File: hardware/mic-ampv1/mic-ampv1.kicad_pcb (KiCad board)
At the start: 2 copper layers, 45.2 x 45 mm, 18 parts, among them J1 XLR3_Switched, U1 NE5532

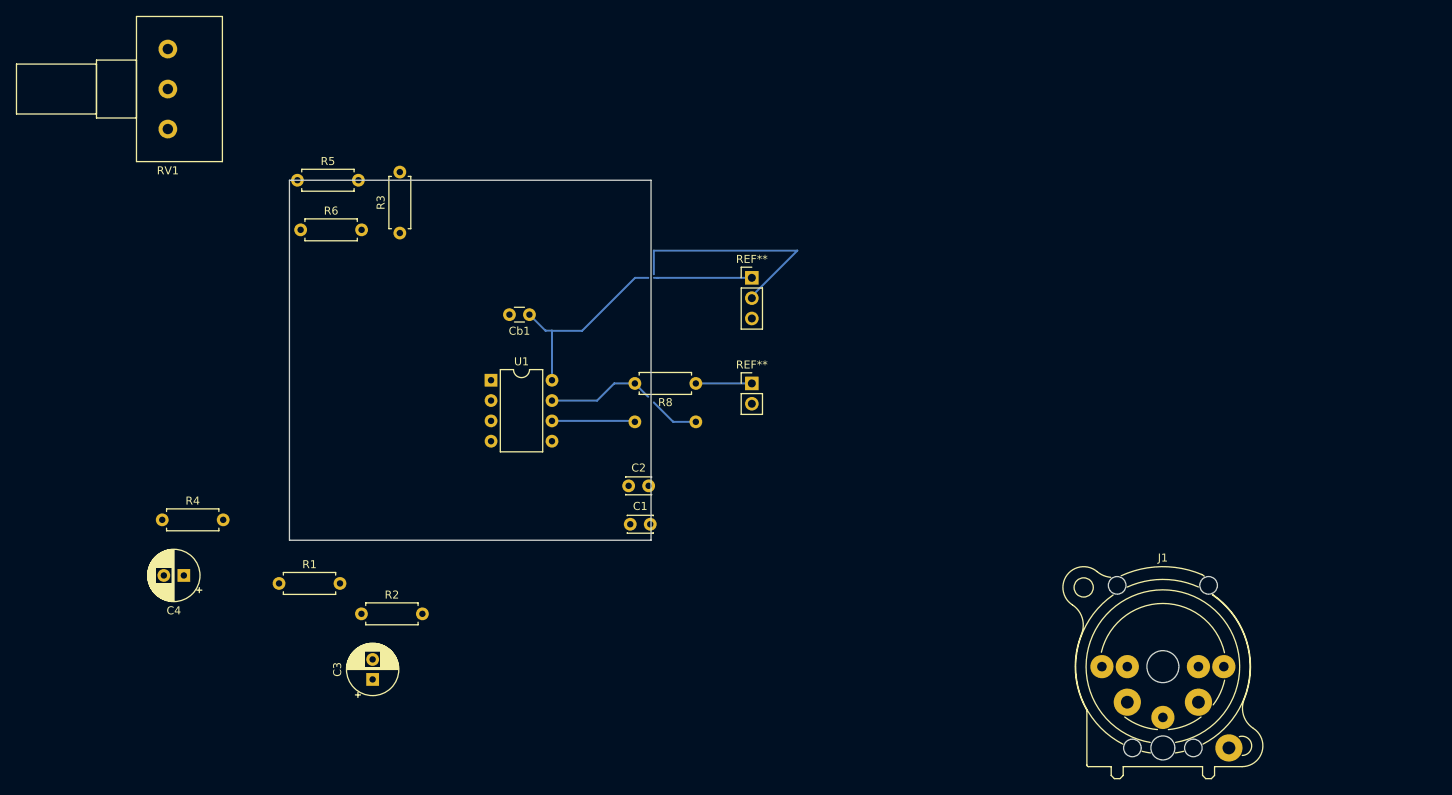
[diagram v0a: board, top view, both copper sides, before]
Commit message: complete pcb for mic
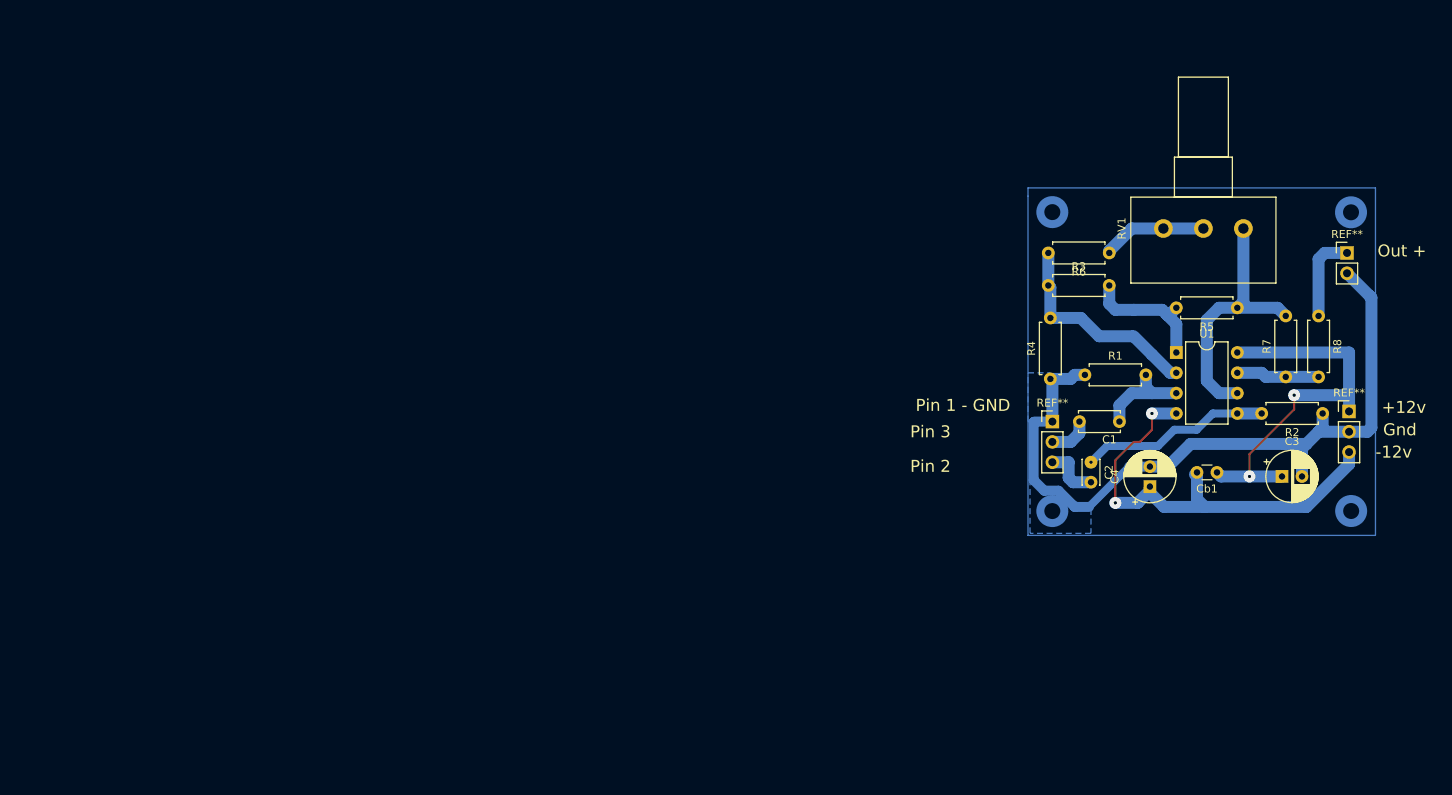
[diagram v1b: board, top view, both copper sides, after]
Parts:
- removed J1: XLR3_Switched, Connector_Audio:Jack_XLR-6.35mm_Neutrik_NCJ6FA-V-0_Vertical
- removed the REF** at (138.2, 72.2)
- added REF**: PinHeader_1x03_P2.54mm_Vertical, Connector_PinHeader_2.54mm:PinHeader_1x03_P2.54mm_Vertical, F.Cu at (175.8, 90.2)
- added REF**: PinHeader_1x03_P2.54mm_Vertical, Connector_PinHeader_2.54mm:PinHeader_1x03_P2.54mm_Vertical, F.Cu at (212.9, 88.9)
- C1: footprint Capacitor_THT:C_Disc_D3.0mm_W2.0mm_P2.50mm -> Capacitor_THT:C_Disc_D5.0mm_W2.5mm_P5.00mm
- R7: moved to F.Cu
- moved RV1 136.3 mm to (199.6, 66.0), turned to 90 degrees
- moved R2 122.7 mm to (209.6, 89.2), turned to 180 degrees
- moved C4 121.3 mm to (188.0, 98.3), turned to 90 degrees
- moved R5 118.6 mm to (198.9, 75.9), turned to 180 degrees
- moved C3 116.5 mm to (204.5, 97.0), turned to 0 degrees
- moved R4 112.4 mm to (175.5, 84.8), turned to 90 degrees
- moved R1 104.1 mm to (179.8, 84.3)
- moved R6 101.1 mm to (182.9, 69.1), turned to 180 degrees
- moved Cb1 88.2 mm to (196.3, 96.5)
- moved U1 85.7 mm to (191.3, 81.5)
- moved R3 81.3 mm to (175.3, 73.2), turned to 0 degrees
- moved R8 78.3 mm to (209.0, 77.0), turned to 270 degrees
- moved REF** 76.2 mm to (212.6, 69.1)
- moved R7 74.0 mm to (204.9, 84.6), turned to 90 degrees
- moved C1 62.5 mm to (184.2, 90.2), turned to 180 degrees
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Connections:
- C3 pad 2: GND -> Gnd
- C4 pad 2: GND -> Gnd
- R1 pad 1: GND -> Gnd
- R2 pad 1: GND -> Gnd
- R4 pad 1: GND -> Gnd
- REF** pad 2: (no net) -> Gnd
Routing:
- net Gnd: track 0.00 -> 97.7 mm
- net -12V: track 29.5 -> 57.2 mm, vias 0 -> 2
- net Net-(R3-Pad1): track 0.00 -> 26.8 mm
- net Net-(C2-Pad1): track 0.00 -> 23.9 mm
- net Net-(R5-Pad1): track 10.4 -> 33.2 mm
- net Net-(R3-Pad2): track 0.00 -> 16.8 mm
- net Net-(R6-Pad1): track 0.00 -> 13.2 mm
- net Net-(C1-Pad1): track 0.00 -> 12.4 mm
- net +12V: track 36.9 -> 49.1 mm, vias 0 -> 2
- net Net-(R7-Pad1): track 19.9 -> 10.4 mm
- net Net-(C1-Pad2): track 0.00 -> 7.06 mm
- net Net-(C2-Pad2): track 0.00 -> 7.00 mm
- net (no net): track 7.00 -> 11.0 mm
- added copper zone on B.Cu, net Gnd
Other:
- board outline removed
- board text added: "+12v"
- board text added: "-12v"
- board text added: "Gnd"
- board text added: "Out +"
- board text added: "Pin 1 - GND"
- board text added: "Pin 2"
- board text added: "Pin 3"

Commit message: Updated mic pre-amp. Longer board to help with layout. increase gain by changing R6 ->47 Ohm
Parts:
- C1: footprint Capacitor_THT:C_Disc_D5.0mm_W2.5mm_P5.00mm -> Capacitor_THT:C_Disc_D3.0mm_W2.0mm_P2.50mm
- R6: value 270 -> 47
- moved C3 7.47 mm to (204.5, 104.5)
- moved C4 7.38 mm to (188.0, 105.7)
- moved C2 3.50 mm to (180.6, 98.8)
- moved C1 1.35 mm to (185.5, 90.2)
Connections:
- R8 pad 1: (no net) -> Out
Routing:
- net Gnd: track 97.7 -> 125.3 mm
- net -12V: track 57.2 -> 73.2 mm
- net Out: track 0.00 -> 11.0 mm
- net (no net): track 11.0 -> 0.00 mm
- net +12V: track 49.1 -> 54.2 mm
- net Net-(C1-Pad2): track 7.06 -> 10.9 mm
- net Net-(U1B-+): track 23.9 -> 21.0 mm
- net Net-(C2-Pad2): track 7.00 -> 9.19 mm
- net Net-(U1A-+): track 12.4 -> 11.8 mm
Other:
- net class Default removed

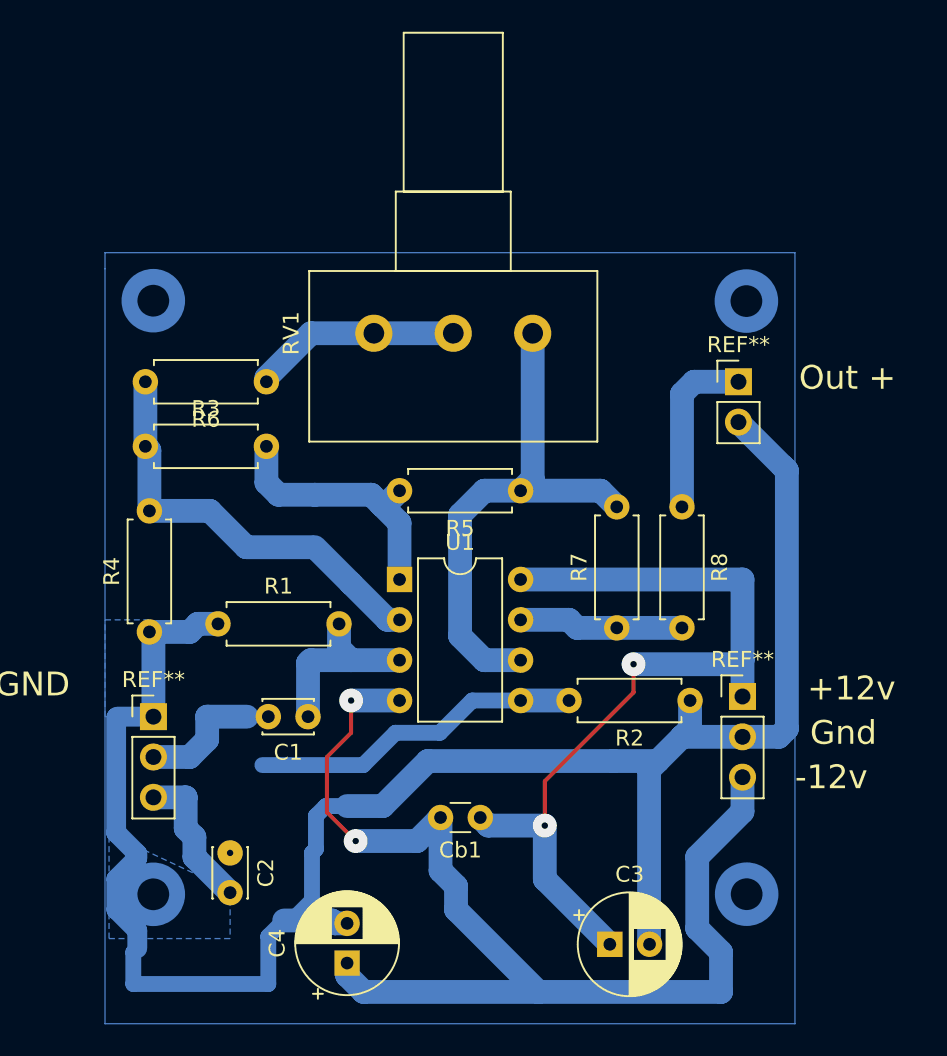
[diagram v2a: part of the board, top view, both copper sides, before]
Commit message: Updated mic preamp. Increased gain. larger PCB
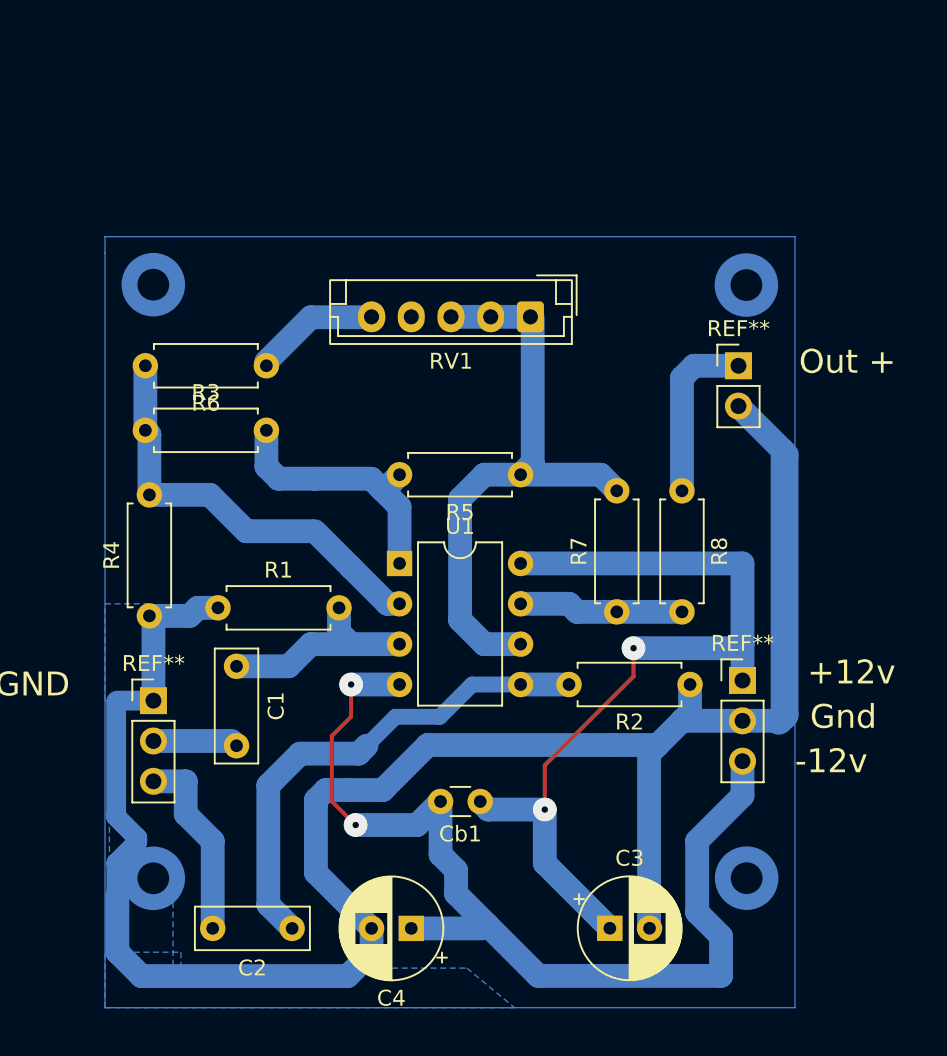
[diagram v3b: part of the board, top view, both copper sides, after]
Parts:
- C1, C2: footprint Capacitor_THT:C_Disc_D3.0mm_W2.0mm_P2.50mm -> Capacitor_THT:C_Rect_L7.0mm_W2.5mm_P5.00mm
- RV1: footprint Potentiometer_THT:Potentiometer_Alps_RK163_Single_Horizontal -> Connector_JST:JST_EH_B5B-EH-A_1x05_P2.50mm_Vertical
- moved C2 6.15 mm to (184.5, 103.5), turned to 180 degrees
- moved C1 5.50 mm to (181.0, 87.0), turned to -90 degrees
- moved C4 4.59 mm to (192.0, 103.5), turned to 180 degrees
- moved RV1 1.04 mm to (199.5, 65.0), turned to 180 degrees
- moved R1 1.01 mm to (179.8, 83.3)
- moved R8 1.01 mm to (209.0, 76.0)
- moved REF** 1.01 mm to (212.9, 87.9)
- moved U1 1.01 mm to (191.3, 80.5)
- moved C3 1.01 mm to (204.5, 103.5)
- moved Cb1 1.01 mm to (196.3, 95.5)
- moved R2 1.01 mm to (209.6, 88.1)
- moved R3 1.01 mm to (175.3, 72.1)
- moved R4 1.01 mm to (175.5, 83.8)
- moved R5 1.01 mm to (198.9, 74.9)
- moved R6 1.01 mm to (182.9, 68.1)
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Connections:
- RV1 pad 2: Net-(R6-Pad1) -> Net-(U1B--)
- RV1 pad 3: Net-(R6-Pad1) -> Net-(U1B--)
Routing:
- net Net-(U1B-+): track 21.0 -> 31.2 mm
- net -12V: track 73.2 -> 64.5 mm
- net Net-(C1-Pad2): track 10.9 -> 5.36 mm
- net Net-(U1B--): track 33.2 -> 38.2 mm
- net Net-(R6-Pad1): track 13.2 -> 8.18 mm
- net Net-(C2-Pad2): track 9.19 -> 12.0 mm
- net Net-(U1A-+): track 11.8 -> 13.4 mm
- net Gnd: track 125.3 -> 124.1 mm
